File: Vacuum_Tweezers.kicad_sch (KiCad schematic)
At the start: 12 parts, among them J101 PnP Interface, J102 PnP Interface, J103 Magnetic Encoder, J104 Limit Switch, J105 TC2050 JTAG, J106 TC2030 PROG, M101 Z-Axis, M102 C-Axis

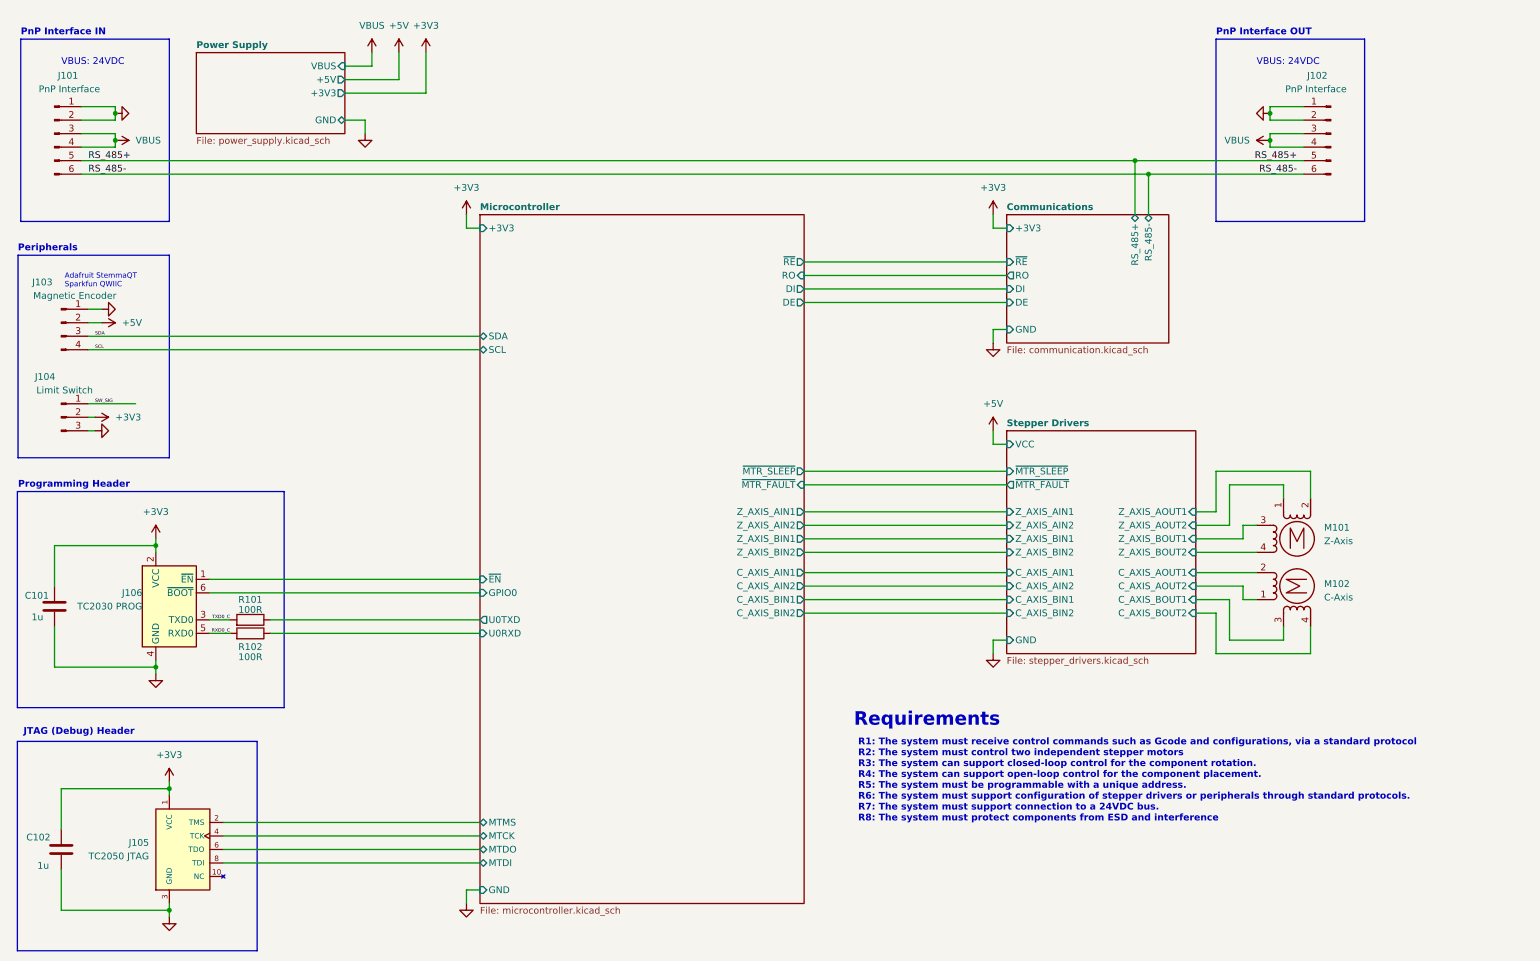
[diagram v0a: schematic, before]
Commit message: Changed motor power supply
Removed 5V power rail. Migrated 3.3V rail to TPS62160
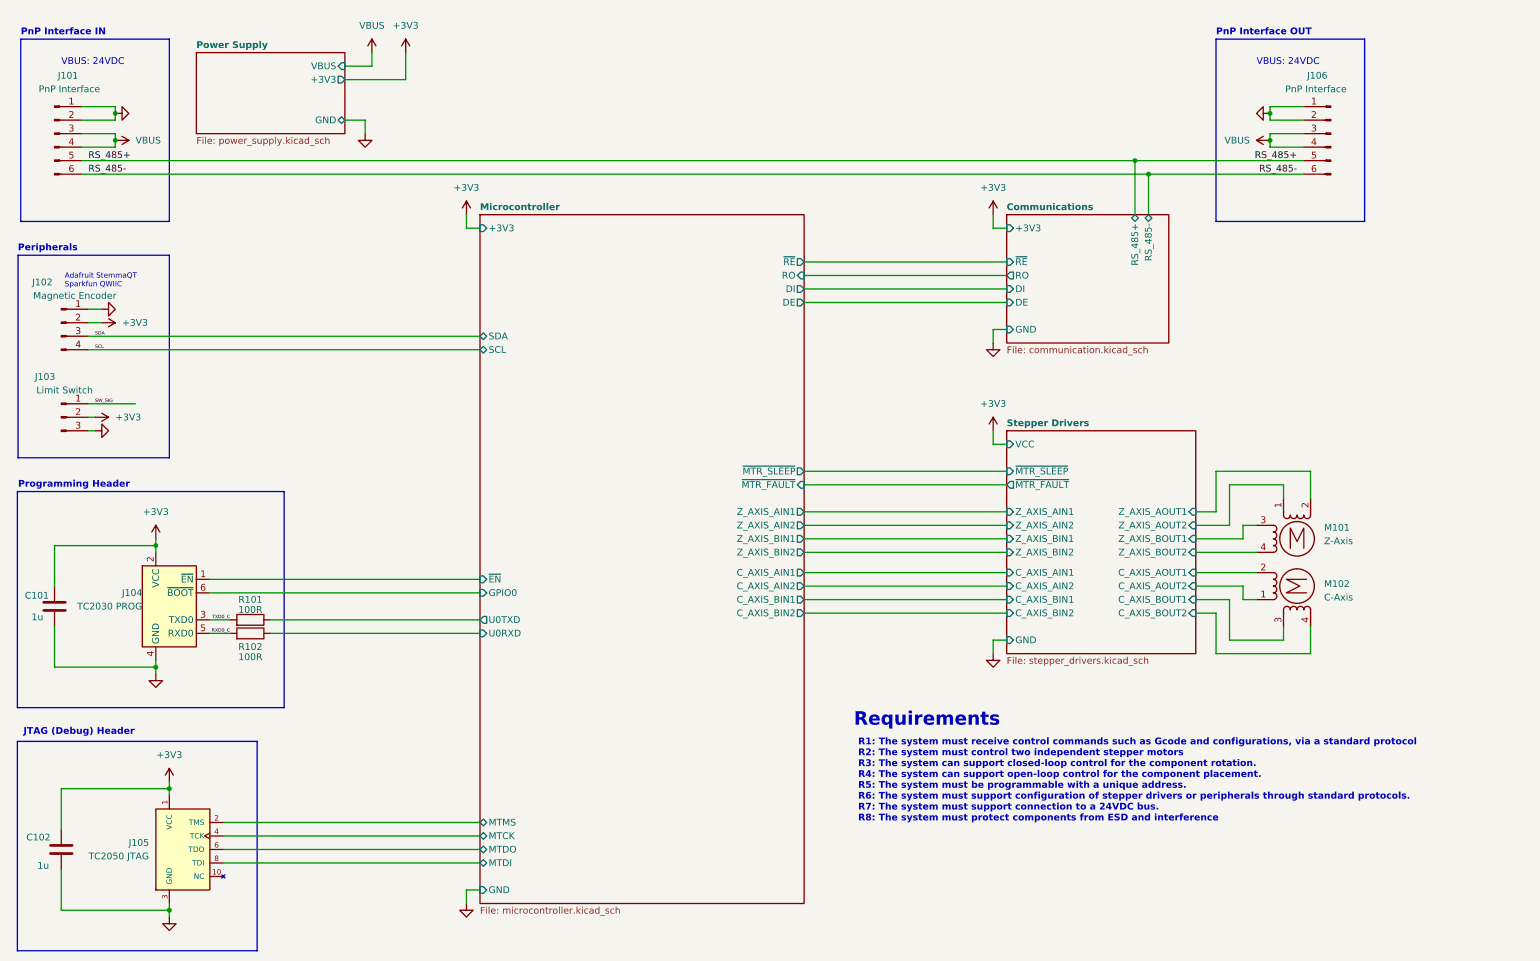
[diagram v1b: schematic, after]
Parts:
- J101: footprint (none) -> Connector_IDC:IDC-Header_2x06_P2.54mm_Vertical
- J102: renamed from J103; footprint Connector_JST:JST_SH_BM04B-SRSS-TB_1x04-1MP_P1.00mm_Vertical -> Connector_JST:JST_SH_SM04B-SRSS-TB_1x04-1MP_P1.00mm_Horizontal
- J103: renamed from J104; footprint Connector_JST:JST_SH_BM03B-SRSS-TB_1x03-1MP_P1.00mm_Vertical -> Connector_JST:JST_SH_SM03B-SRSS-TB_1x03-1MP_P1.00mm_Horizontal
- J106: renamed from J102; footprint (none) -> Connector_IDC:IDC-Header_2x06_P2.54mm_Vertical
- M101, M102: footprint (none) -> Connector_JST:JST_PH_S4B-PH-SM4-TB_1x04-1MP_P2.00mm_Horizontal
- renumbered J106 to J104
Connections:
- net +5V is gone; now on net +3V3: J102.2 (Pin_2)
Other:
- sheet Power Supply ports: added none; removed +5V

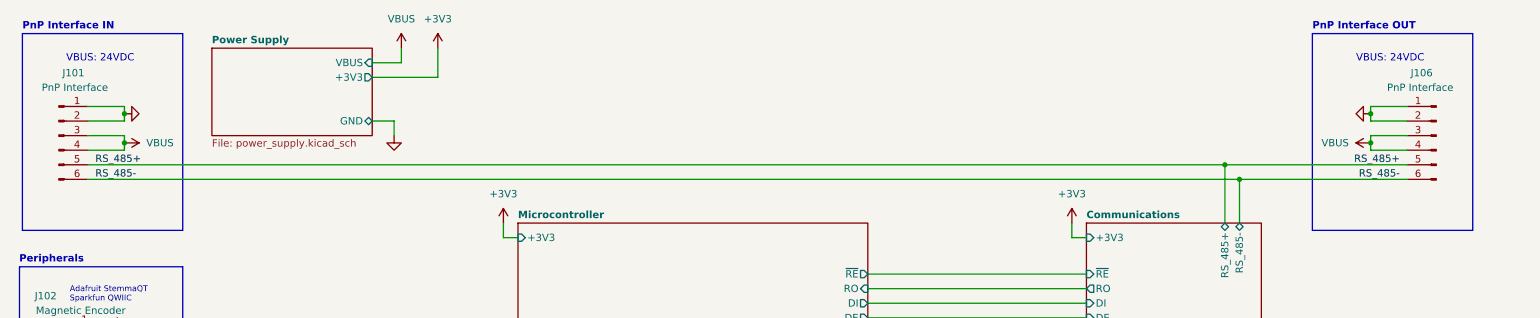
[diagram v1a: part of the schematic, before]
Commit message: Changed footprints
Modified some footprints to better fit layout and part availability
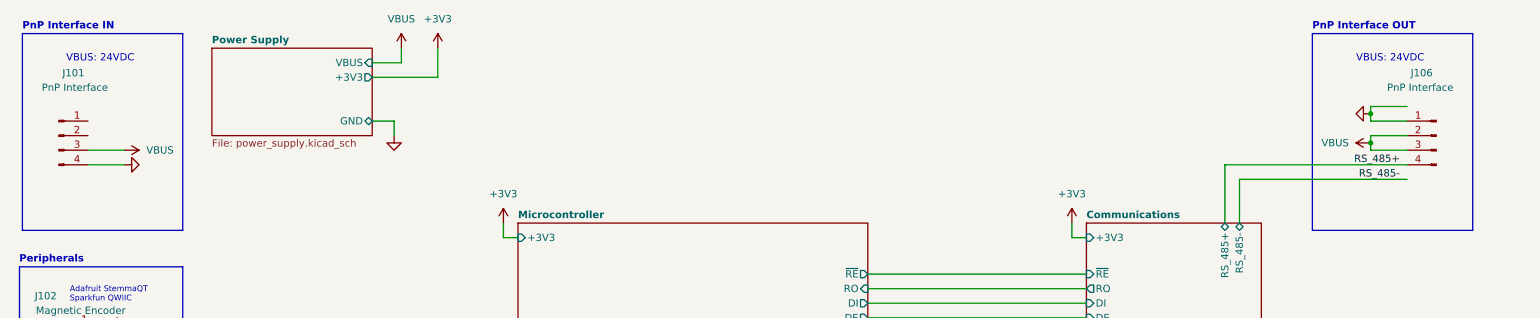
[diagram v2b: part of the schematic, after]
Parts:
- J101, J106: footprint Connector_IDC:IDC-Header_2x06_P2.54mm_Vertical -> Connector_JST:JST_PH_B4B-PH-SM4-TB_1x04-1MP_P2.00mm_Vertical; symbol Connector:Conn_01x06_Pin -> Connector:Conn_01x04_Pin
- M101, M102: footprint Connector_JST:JST_PH_S4B-PH-SM4-TB_1x04-1MP_P2.00mm_Horizontal -> Connector_Molex:Molex_PicoBlade_53261-0471_1x04-1MP_P1.25mm_Horizontal
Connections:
- net GND: now also J101.4 (Pin_4); no longer J101.1 (Pin_1), J101.2 (Pin_2), J106.2 (Pin_2)
- net RS_485+: now also J106.4 (Pin_4); no longer J101.5 (Pin_5), J106.5 (Pin_5)
- net RS_485-: no longer J101.6 (Pin_6), J106.6 (Pin_6)
- net VBUS: now also J106.2 (Pin_2); no longer J101.4 (Pin_4), J106.4 (Pin_4)
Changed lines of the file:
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@@
 	)
 	(junction
-		(at 38.1 31.75)
-		(diameter 0)
-		(color 0 0 0 0)
-	)
-	(junction
 		(at 48.26 158.75)
 		(diameter 0)
@@
 	)
 	(junction
-		(at 232.41 43.18)
-		(diameter 0)
-		(color 0 0 0 0)
-	)
-	(junction
 		(at 45.72 135.89)
 		(diameter 0)
@@
 	)
 	(junction
-		(at 229.87 40.64)
-		(diameter 0)
-		(color 0 0 0 0)
-	)
-	(junction
-		(at 38.1 36.83)
-		(diameter 0)
-		(color 0 0 0 0)
-	)
-	(junction
 		(at 48.26 181.61)
 		(diameter 0)
@@
 	(wire
 		(pts
-			(xy 31.75 40.64) (xy 229.87 40.64)
-		)
-		(stroke
-			(width 0)
-			(type default)
-		)
-	)
-	(wire
-		(pts
 			(xy 257.81 130.81) (xy 257.81 128.27)
 		)
@@
 	(wire
 		(pts
-			(xy 31.75 30.48) (xy 38.1 30.48)
-		)
-		(stroke
-			(width 0)
-			(type default)
-		)
-	)
-	(wire
-		(pts
 			(xy 261.62 38.1) (xy 255.27 38.1)
 		)
@@
 	(wire
 		(pts
-			(xy 38.1 36.83) (xy 38.1 35.56)
-		)
-		(stroke
-			(width 0)
-			(type default)
-		)
-	)
-	(wire
-		(pts
 			(xy 81.28 25.4) (xy 92.71 25.4)
 		)
@@
 	(wire
 		(pts
-			(xy 38.1 33.02) (xy 38.1 31.75)
-		)
-		(stroke
-			(width 0)
-			(type default)
-		)
-	)
-	(wire
-		(pts
-			(xy 38.1 38.1) (xy 38.1 36.83)
-		)
-		(stroke
-			(width 0)
-			(type default)
-		)
-	)
-	(wire
-		(pts
 			(xy 86.36 20.32) (xy 86.36 22.86)
 		)
@@
 	(wire
 		(pts
-			(xy 31.75 43.18) (xy 232.41 43.18)
-		)
-		(stroke
-			(width 0)
-			(type default)
-		)
-	)
-	(wire
-		(pts
 			(xy 27.94 173.99) (xy 27.94 181.61)
 		)
@@
 	(wire
 		(pts
-			(xy 31.75 38.1) (xy 38.1 38.1)
-		)
-		(stroke
-			(width 0)
-			(type default)
-		)
-	)
-	(wire
-		(pts
 			(xy 241.3 123.19) (xy 247.65 123.19)
 		)
@@
 	(wire
 		(pts
-			(xy 167.64 99.06) (xy 205.74 99.06)
+			(xy 31.75 38.1) (xy 38.1 38.1)
 		)
 		(stroke
@@
 	(wire
 		(pts
-			(xy 31.75 35.56) (xy 38.1 35.56)
+			(xy 167.64 99.06) (xy 205.74 99.06)
 		)
 		(stroke
@@
 	(wire
 		(pts
-			(xy 38.1 31.75) (xy 38.1 30.48)
+			(xy 247.65 109.22) (xy 247.65 101.6)
 		)
 		(stroke
@@
 	(wire
 		(pts
-			(xy 247.65 109.22) (xy 247.65 101.6)
+			(xy 31.75 40.64) (xy 38.1 40.64)
 		)
 		(stroke
@@
 	(wire
 		(pts
-			(xy 31.75 33.02) (xy 38.1 33.02)
-		)
-		(stroke
-			(width 0)
-			(type default)
-		)
-	)
-	(wire
-		(pts
 			(xy 247.65 101.6) (xy 257.81 101.6)
 		)
@@
 		)
 	)
-	(label "RS_485-"
-		(at 33.02 43.18 0)
-		(fields_autoplaced yes)
-		(effects
-			(font
-				(size 1.27 1.27)
-			)
-			(justify left bottom)
-		)
-	)
 	(label "RXD0_C"
 		(at 59.69 129.54 180)
@@
 		)
 	)
-	(label "RS_485+"
-		(at 33.02 40.64 0)
-		(fields_autoplaced yes)
-		(effects
-			(font
-				(size 1.27 1.27)
-			)
-			(justify left bottom)
-		)
-	)
 	(symbol
 		(lib_id "Device:C")
@@
 			)
 		)
-		(property "Footprint" "Connector_JST:JST_PH_S4B-PH-SM4-TB_1x04-1MP_P2.00mm_Horizontal"
+		(property "Footprint" "Connector_Molex:Molex_PicoBlade_53261-0471_1x04-1MP_P1.25mm_Horizontal"
 			(at 260.604 112.014 0)
 			(effects
@@
 	)
 	(symbol
-		(lib_id "Connector:Conn_01x06_Pin")
+		(lib_id "Connector:Conn_01x04_Pin")
 		(at 26.67 35.56 0)
 		(unit 1)
@@
 			)
 		)
-		(property "Footprint" "Connector_IDC:IDC-Header_2x06_P2.54mm_Vertical"
+		(property "Footprint" "Connector_JST:JST_PH_B4B-PH-SM4-TB_1x04-1MP_P2.00mm_Vertical"
 			(at 26.67 35.56 0)
 			(effects
@@
 			)
 		)
-		(property "Description" "Generic connector, single row, 01x06, script generated"
+		(property "Description" "Generic connector, single row, 01x04, script generated"
 			(at 26.67 35.56 0)
 			(effects
@@
 		(pin "4"
 		)
-		(pin "6"
-		)
-		(pin "5"
-		)
 		(instances
 			(project "Vacuum_Tweezers"
@@
 			)
 		)
-		(property "Footprint" "Connector_JST:JST_PH_S4B-PH-SM4-TB_1x04-1MP_P2.00mm_Horizontal"
+		(property "Footprint" "Connector_Molex:Molex_PicoBlade_53261-0471_1x04-1MP_P1.25mm_Horizontal"
 			(at 260.604 120.396 0)
 			(effects
@@
 	)
 	(symbol
-		(lib_id "Connector:Conn_01x06_Pin")
+		(lib_id "power:GND")
+		(at 38.1 40.64 90)
+		(unit 1)
+		(exclude_from_sim no)
+		(in_bom yes)
+		(on_board yes)
+		(dnp no)
+		(fields_autoplaced yes)
+		(property "Reference" "#PWR0105"
+			(at 44.45 40.64 0)
+			(effects
+				(font
+					(size 1.27 1.27)
+				)
+				(hide yes)
+			)
+		)
+		(property "Value" "GND"
+			(at 41.91 40.6399 90)
+			(effects
+				(font
+					(size 1.27 1.27)
+				)
+				(justify right)
+				(hide yes)
+			)
+		)
+		(property "Footprint" ""
+			(at 38.1 40.64 0)
+			(effects
+				(font
+					(size 1.27 1.27)
+				)
+				(hide yes)
+			)
+		)
+		(property "Datasheet" ""
+			(at 38.1 40.64 0)
+			(effects
+				(font
+					(size 1.27 1.27)
+				)
+				(hide yes)
+			)
+		)
+		(property "Description" "Power symbol creates a global label with name \"GND\" , ground"
+			(at 38.1 40.64 0)
+			(effects
+				(font
+					(size 1.27 1.27)
+				)
+				(hide yes)
+			)
+		)
+		(pin "1"
+		)
+		(instances
+			(project "Vacuum_Tweezers"
+				(path "/25b5e35e-9397-4bb5-a91c-fc11ba49a08d"
+					(reference "#PWR0105")
+					(unit 1)
+				)
+			)
+		)
+	)
+	(symbol
+		(lib_id "Connector:Conn_01x04_Pin")
 		(at 266.7 35.56 0)
 		(mirror y)
@@
 			)
 		)
-		(property "Footprint" "Connector_IDC:IDC-Header_2x06_P2.54mm_Vertical"
+		(property "Footprint" "Connector_JST:JST_PH_B4B-PH-SM4-TB_1x04-1MP_P2.00mm_Vertical"
 			(at 266.7 35.56 0)
 			(effects
@@
 			)
 		)
-		(property "Description" "Generic connector, single row, 01x06, script generated"
+		(property "Description" "Generic connector, single row, 01x04, script generated"
 			(at 266.7 35.56 0)
 			(effects
@@
 		(pin "4"
 		)
-		(pin "6"
-		)
-		(pin "5"
-		)
 		(instances
 			(project "Vacuum_Tweezers"
@@
 	)
 	(symbol
-		(lib_id "power:GND")
-		(at 38.1 31.75 90)
-		(unit 1)
-		(exclude_from_sim no)
-		(in_bom yes)
-		(on_board yes)
-		(dnp no)
-		(fields_autoplaced yes)
-		(property "Reference" "#PWR0105"
-			(at 44.45 31.75 0)
-			(effects
-				(font
-					(size 1.27 1.27)
-				)
-				(hide yes)
-			)
-		)
-		(property "Value" "GND"
-			(at 41.91 31.7499 90)
-			(effects
-				(font
-					(size 1.27 1.27)
-				)
-				(justify right)
-				(hide yes)
-			)
-		)
-		(property "Footprint" ""
-			(at 38.1 31.75 0)
-			(effects
-				(font
-					(size 1.27 1.27)
-				)
-				(hide yes)
-			)
-		)
-		(property "Datasheet" ""
-			(at 38.1 31.75 0)
-			(effects
-				(font
-					(size 1.27 1.27)
-				)
-				(hide yes)
-			)
-		)
-		(property "Description" "Power symbol creates a global label with name \"GND\" , ground"
-			(at 38.1 31.75 0)
-			(effects
-				(font
-					(size 1.27 1.27)
-				)
-				(hide yes)
-			)
-		)
-		(pin "1"
-		)
-		(instances
-			(project "Vacuum_Tweezers"
-				(path "/25b5e35e-9397-4bb5-a91c-fc11ba49a08d"
-					(reference "#PWR0105")
-					(unit 1)
-				)
-			)
-		)
-	)
-	(symbol
 		(lib_id "Connector:Conn_01x04_Pin")
 		(at 27.94 71.12 0)
@@
 	(symbol
 		(lib_id "power:VBUS")
-		(at 38.1 36.83 270)
+		(at 38.1 38.1 270)
 		(unit 1)
 		(exclude_from_sim no)
@@
 		(fields_autoplaced yes)
 		(property "Reference" "#PWR0106"
-			(at 34.29 36.83 0)
+			(at 34.29 38.1 0)
 			(effects
 				(font
@@
 		)
 		(property "Value" "VBUS"
-			(at 41.91 36.8299 90)
+			(at 41.91 38.0999 90)
 			(effects
 				(font
@@
 		)
 		(property "Footprint" ""
-			(at 38.1 36.83 0)
+			(at 38.1 38.1 0)
 			(effects
 				(font
@@
 		)
 		(property "Datasheet" ""
-			(at 38.1 36.83 0)
+			(at 38.1 38.1 0)
 			(effects
 				(font
@@
 		)
 		(property "Description" "Power symbol creates a global label with name \"VBUS\""
-			(at 38.1 36.83 0)
+			(at 38.1 38.1 0)
 			(effects
 				(font

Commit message: Finished Rev A1 PCB
Added all components and routed parts for Rev A1 PCB
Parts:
- added J107: Valve Coil, Connector_JST:JST_SH_SM02B-SRSS-TB_1x02-1MP_P1.00mm_Horizontal, symbol Connector:Conn_01x02_Pin
- J101, J106: footprint Connector_JST:JST_PH_B4B-PH-SM4-TB_1x04-1MP_P2.00mm_Vertical -> Connector_JST:JST_PH_S6B-PH-SM4-TB_1x06-1MP_P2.00mm_Horizontal; symbol Connector:Conn_01x04_Pin -> Connector:Conn_01x06_Pin
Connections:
- net GND: now also J101.1 (Pin_1), J101.2 (Pin_2), J106.2 (Pin_2); no longer J101.4 (Pin_4)
- net RS_485+: now also J101.5 (Pin_5), J106.5 (Pin_5); no longer J106.4 (Pin_4)
- net RS_485-: now also J101.6 (Pin_6), J106.6 (Pin_6)
- net Stepper Drivers/C_AXIS_AOUT1: now also M102.1; no longer M102.2 (-)
- net Stepper Drivers/C_AXIS_AOUT2: now also M102.2 (-); no longer M102.1
- net Stepper Drivers/C_AXIS_BOUT1: now also M102.4; no longer M102.3
- net Stepper Drivers/C_AXIS_BOUT2: now also M102.3; no longer M102.4
- net Stepper Drivers/Z_AXIS_AOUT1: now also M101.1; no longer M101.2 (-)
- net Stepper Drivers/Z_AXIS_AOUT2: now also M101.2 (-); no longer M101.1
- net Stepper Drivers/Z_AXIS_BOUT1: now also M101.4; no longer M101.3
- net Stepper Drivers/Z_AXIS_BOUT2: now also M101.3; no longer M101.4
- net VBUS: now also J101.4 (Pin_4), J106.4 (Pin_4); no longer J106.2 (Pin_2)
- new net Solenoid Driver/COIL_NEG: J107.2 (Pin_2)
- new net Solenoid Driver/COIL_POS: J107.1 (Pin_1)
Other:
- added sheet Solenoid Driver (solenoid_driver.kicad_sch)
- sheet Microcontroller ports: added VALVE_CTRL; removed none
- note added: "VBUS: 24VDC Imax: 2A per pin Iexpected: 1A"
- note removed: "VBUS: 24VDC"
- moved on the sheet: M101, M102
